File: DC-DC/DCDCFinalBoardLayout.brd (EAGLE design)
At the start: 152.3 x 128 mm, 39 parts, among them K1 ALZ12B12W

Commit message: updated gerber files with new diode
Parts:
- removed BUCKPROTECTDIODE, RELAYPROTECTDIODE, VARBUCKPROTECTDIODE: SL44HE3, diode:SMC
- added Q1, Q2: BUZ10, transistor-fet:TO220
- moved BMSOUTFUSE 16.3 mm to (35.2, 168.5), turned to 0 degrees
- moved VARMPFUSE 13.5 mm to (49.0, 168.1)
- moved FANFUSE 9.52 mm to (65.4, 167.6)
- moved VARMP 4.19 mm to (33.3, 178.8)
- moved FANS 3.42 mm to (55.4, 178.7)
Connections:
- net 12V: now also Q1.2, Q2.2; no longer BUCKPROTECTDIODE.C, RELAYPROTECTDIODE.C, VARBUCKPROTECTDIODE.C
- net N$13: now also Q1.1; no longer VARBUCKPROTECTDIODE.A
- net N$15: now also Q2.1; no longer BUCKPROTECTDIODE.A
- net N$4: now also Q2.3; no longer RELAYPROTECTDIODE.A
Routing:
- net GND: track 369.5 -> 8.27 mm
- net N$15: track 108.7 -> 157.1 mm, vias 1 -> 2
- net N$4: track 168.3 -> 195.8 mm
- net N$10: track 10.2 -> 23.0 mm
- net N$13: track 146.8 -> 158.9 mm
- net 12V: track 302.3 -> 307.1 mm
- net N$8: track 11.5 -> 15.4 mm
- net N$6: track 10.7 -> 14.3 mm

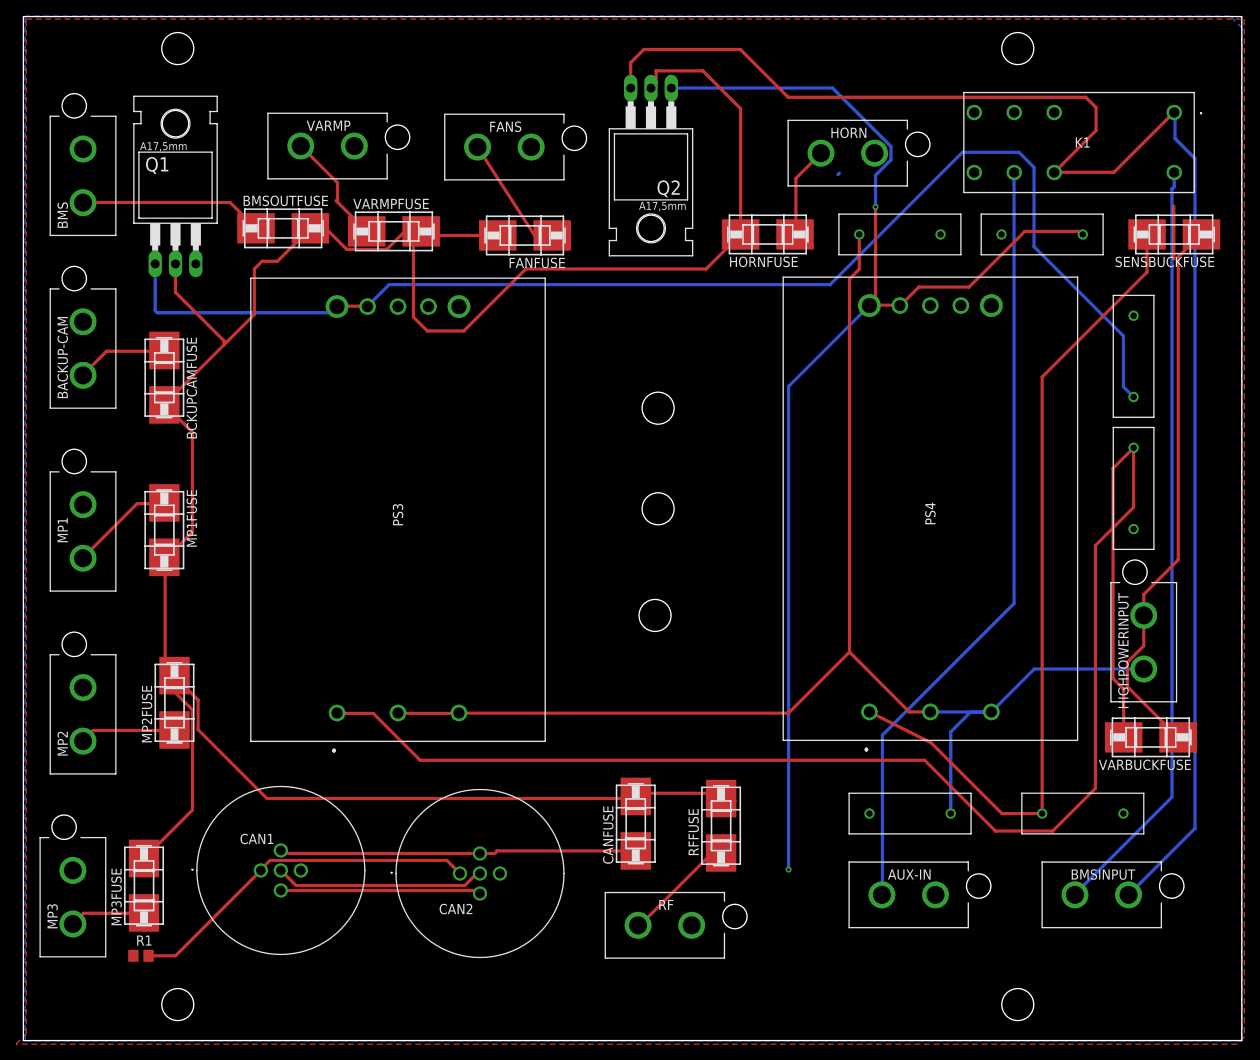
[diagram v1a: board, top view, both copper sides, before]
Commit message: updated DCDC diode
replaced insufficient SMD diode (in terms of current cap) with three TO220 diodes, with parallel dual configurations
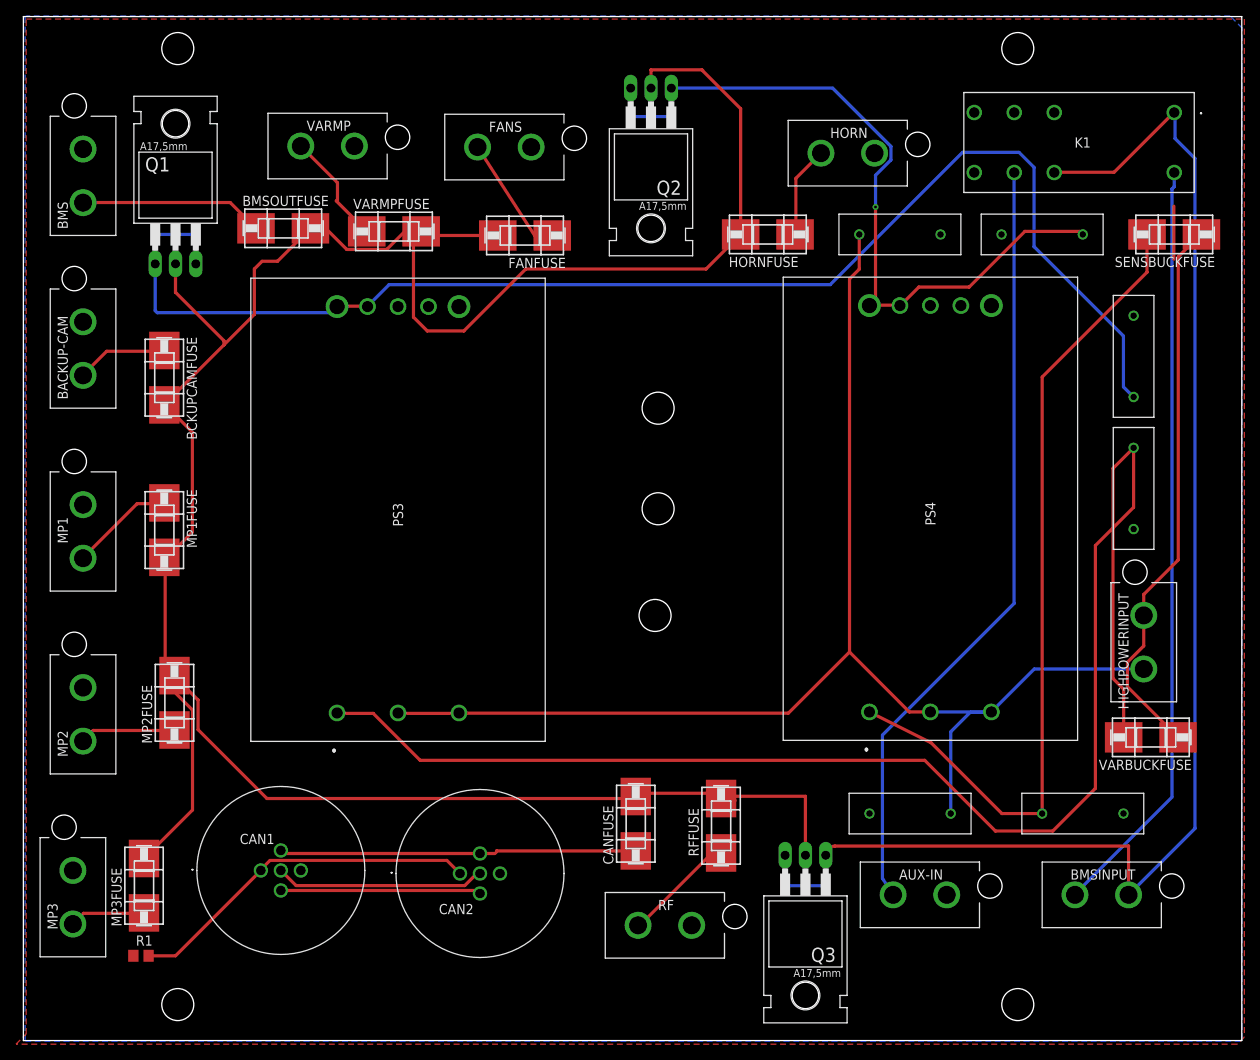
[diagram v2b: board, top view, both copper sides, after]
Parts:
- added Q3: BUZ10, transistor-fet:TO220
- moved AUX-IN 1.40 mm to (107.3, 85.2)
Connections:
- net 12V: now also Q3.2
- net N$13: now also Q1.3
- net N$15: now also Q2.3
- net N$4: now also Q3.1, Q3.3; no longer Q2.3
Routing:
- net N$15: track 157.1 -> 94.4 mm, vias 2 -> 1
- net 12V: track 307.1 -> 325.7 mm
- net N$4: track 195.8 -> 177.8 mm
- net N$13: track 158.9 -> 171.5 mm
